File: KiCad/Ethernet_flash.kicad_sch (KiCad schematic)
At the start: 28 parts, among them IC10 MX25UM25645GXDI00-T, IC8 TFP410PAP, IC9 TS3DV642A0RUAR

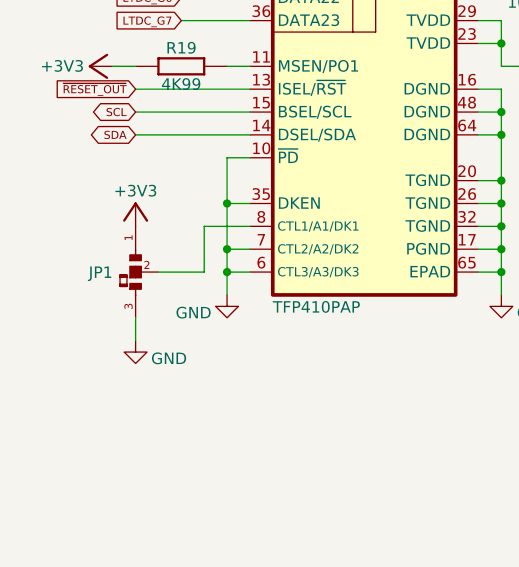
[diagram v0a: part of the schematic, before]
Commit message: JP1 type modifed
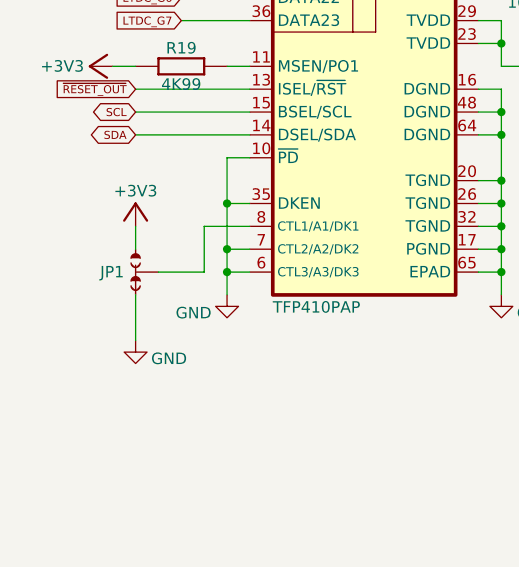
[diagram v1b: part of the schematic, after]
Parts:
- JP1: footprint PCM_EEZ_SMD:JP3 shorted with 0R (0603) 2-3 -> PCM_EEZ_SMD:JP3 shorted (0603); symbol PCM_EEZ_unsorted:JP3 shorted with 0R (2-3) -> PCM_EEZ_unsorted:JP3 shorted
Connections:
- net +3V3: now also JP1.NO; no longer JP1.1
- net GND: now also JP1.NC; no longer JP1.3
- net at IC8.8 (CTL1/A1/DK1): now also JP1.COM; no longer JP1.2
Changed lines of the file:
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@@
 	(wire
 		(pts
+			(xy 22.86 142.24) (xy 22.86 144.78)
+		)
+		(stroke
+			(width 0)
+			(type default)
+		)
+	)
+	(wire
+		(pts
 			(xy 30.48 43.18) (xy 35.56 43.18)
 		)
@@
 	(wire
 		(pts
-			(xy 22.86 152.4) (xy 22.86 154.94)
-		)
-		(stroke
-			(width 0)
-			(type default)
-		)
-	)
-	(wire
-		(pts
 			(xy 60.96 63.5) (xy 68.58 63.5)
 		)
@@
 	(wire
 		(pts
+			(xy 22.86 149.86) (xy 22.86 154.94)
+		)
+		(stroke
+			(width 0)
+			(type default)
+		)
+	)
+	(wire
+		(pts
 			(xy 60.96 43.18) (xy 68.58 43.18)
 		)
@@
 	)
 	(symbol
-		(lib_id "PCM_EEZ_unsorted:JP3 shorted with 0R (2-3)")
-		(at 22.86 147.32 90)
-		(mirror x)
+		(lib_id "PCM_EEZ_unsorted:JP3 shorted")
+		(at 22.86 147.32 0)
 		(unit 1)
 		(exclude_from_sim no)
@@
 		(on_board yes)
 		(dnp no)
-		(fields_autoplaced yes)
 		(property "Reference" "JP1"
-			(at 20.32 147.3834 90)
+			(at 21.59 147.3199 0)
 			(effects
 				(font
 					(size 1.27 1.27)
 				)
-				(justify left)
+				(justify right)
 			)
 		)
@@
 			)
 		)
-		(property "Footprint" "PCM_EEZ_SMD:JP3 shorted with 0R (0603) 2-3"
-			(at 26.67 147.32 0)
+		(property "Footprint" "PCM_EEZ_SMD:JP3 shorted (0603)"
+			(at 22.86 152.4 0)
 			(effects
 				(font
@@
 		)
 		(property "Datasheet" ""
-			(at 22.86 147.32 90)
+			(at 22.86 147.32 0)
 			(effects
 				(font
@@
 			)
 		)
-		(pin "1"
+		(property "DigiKey" ""
+			(at 22.86 147.32 0)
+			(effects
+				(font
+					(size 1.27 1.27)
+				)
+				(hide yes)
+			)
 		)
-		(pin "3"
+		(property "Mouser" ""
+			(at 22.86 147.32 0)
+			(effects
+				(font
+					(size 1.27 1.27)
+				)
+				(hide yes)
+			)
 		)
-		(pin "2"
+		(property "TME" ""
+			(at 22.86 147.32 0)
+			(effects
+				(font
+					(size 1.27 1.27)
+				)
+				(hide yes)
+			)
+		)
+		(property "LCSC" ""
+			(at 22.86 147.32 0)
+			(effects
+				(font
+					(size 1.27 1.27)
+				)
+				(hide yes)
+			)
+		)
+		(pin "COM"
+		)
+		(pin "NC"
+		)
+		(pin "NO"
 		)
 		(instances

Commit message: Folders paths adjusted, Cin added to 3V3 LDO
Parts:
- renumbered C60 to C61, C61 to C62, C62 to C63, C63 to C64, C64 to C65, C65 to C66, C66 to C67, C67 to C68, C68 to C69, C69 to C70, C70 to C71, C71 to C72, C72 to C73, C73 to C74, C74 to C75
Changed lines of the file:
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@@
 	(title_block
 		(title "${project_name}")
-		(date "2025-11-02")
+		(date "2025-11-03")
 		(rev "${project_version}")
 		(company "${project_creator}")
@@
 		(on_board yes)
 		(dnp no)
-		(property "Reference" "C61"
+		(property "Reference" "C62"
 			(at 68.58 114.3 0)
 			(effects
@@
 			(project "BB3plus CM5 STM32H7 module"
 				(path "/1a4f0aea-3a69-423f-8790-3103cd0321c4/6c545e17-ca5e-4b04-9dff-4169dbe59c9e"
-					(reference "C61")
+					(reference "C62")
 					(unit 1)
 				)
@@
 		(on_board yes)
 		(dnp no)
-		(property "Reference" "C71"
+		(property "Reference" "C72"
 			(at 256.54 38.1 0)
 			(effects
@@
 			(project "BB3plus CM5 STM32H7 module"
 				(path "/1a4f0aea-3a69-423f-8790-3103cd0321c4/6c545e17-ca5e-4b04-9dff-4169dbe59c9e"
-					(reference "C71")
+					(reference "C72")
 					(unit 1)
 				)
@@
 		(on_board yes)
 		(dnp no)
-		(property "Reference" "C64"
+		(property "Reference" "C65"
 			(at 73.66 127 0)
 			(effects
@@
 			(project "BB3plus CM5 STM32H7 module"
 				(path "/1a4f0aea-3a69-423f-8790-3103cd0321c4/6c545e17-ca5e-4b04-9dff-4169dbe59c9e"
-					(reference "C64")
+					(reference "C65")
 					(unit 1)
 				)
@@
 		(on_board yes)
 		(dnp no)
-		(property "Reference" "C72"
+		(property "Reference" "C73"
 			(at 261.62 38.1 0)
 			(effects
@@
 			(project "BB3plus CM5 STM32H7 module"
 				(path "/1a4f0aea-3a69-423f-8790-3103cd0321c4/6c545e17-ca5e-4b04-9dff-4169dbe59c9e"
-					(reference "C72")
+					(reference "C73")
 					(unit 1)
 				)
@@
 		(on_board yes)
 		(dnp no)
-		(property "Reference" "#PWR015"
+		(property "Reference" "#PWR016"
 			(at 198.12 29.21 0)
 			(effects
@@
 			(project "BB3plus CM5 STM32H7 module"
 				(path "/1a4f0aea-3a69-423f-8790-3103cd0321c4/6c545e17-ca5e-4b04-9dff-4169dbe59c9e"
-					(reference "#PWR015")
+					(reference "#PWR016")
 					(unit 1)
 				)
@@
 		(on_board yes)
 		(dnp no)
-		(property "Reference" "C60"
+		(property "Reference" "C61"
 			(at 68.58 101.6 0)
 			(effects
@@
 			(project "BB3plus CM5 STM32H7 module"
 				(path "/1a4f0aea-3a69-423f-8790-3103cd0321c4/6c545e17-ca5e-4b04-9dff-4169dbe59c9e"
-					(reference "C60")
+					(reference "C61")
 					(unit 1)
 				)
@@
 		(on_board yes)
 		(dnp no)
-		(property "Reference" "C65"
+		(property "Reference" "C66"
 			(at 78.74 101.6 0)
 			(effects
@@
 			(project "BB3plus CM5 STM32H7 module"
 				(path "/1a4f0aea-3a69-423f-8790-3103cd0321c4/6c545e17-ca5e-4b04-9dff-4169dbe59c9e"
-					(reference "C65")
+					(reference "C66")
 					(unit 1)
 				)
@@
 		(on_board yes)
 		(dnp no)
-		(property "Reference" "C63"
+		(property "Reference" "C64"
 			(at 73.66 101.6 0)
 			(effects
@@
 			(project "BB3plus CM5 STM32H7 module"
 				(path "/1a4f0aea-3a69-423f-8790-3103cd0321c4/6c545e17-ca5e-4b04-9dff-4169dbe59c9e"
-					(reference "C63")
+					(reference "C64")
 					(unit 1)
 				)
@@
 		(on_board yes)
 		(dnp no)
-		(property "Reference" "C73"
+		(property "Reference" "C74"
 			(at 269.24 38.1 0)
 			(effects
@@
 			(project "BB3plus CM5 STM32H7 module"
 				(path "/1a4f0aea-3a69-423f-8790-3103cd0321c4/6c545e17-ca5e-4b04-9dff-4169dbe59c9e"
-					(reference "C73")
+					(reference "C74")
 					(unit 1)
 				)
@@
 		(on_board yes)
 		(dnp no)
-		(property "Reference" "C66"
+		(property "Reference" "C67"
 			(at 93.98 101.6 0)
 			(effects
@@
 			(project "BB3plus CM5 STM32H7 module"
 				(path "/1a4f0aea-3a69-423f-8790-3103cd0321c4/6c545e17-ca5e-4b04-9dff-4169dbe59c9e"
-					(reference "C66")
+					(reference "C67")
 					(unit 1)
 				)
@@
 		(on_board yes)
 		(dnp no)
-		(property "Reference" "C70"
+		(property "Reference" "C71"
 			(at 248.92 38.1 0)
 			(effects
@@
 			(project "BB3plus CM5 STM32H7 module"
 				(path "/1a4f0aea-3a69-423f-8790-3103cd0321c4/6c545e17-ca5e-4b04-9dff-4169dbe59c9e"
-					(reference "C70")
+					(reference "C71")
 					(unit 1)
 				)
@@
 		(on_board yes)
 		(dnp no)
-		(property "Reference" "C62"
+		(property "Reference" "C63"
 			(at 68.58 127 0)
 			(effects
@@
 			(project "BB3plus CM5 STM32H7 module"
 				(path "/1a4f0aea-3a69-423f-8790-3103cd0321c4/6c545e17-ca5e-4b04-9dff-4169dbe59c9e"
-					(reference "C62")
+					(reference "C63")
 					(unit 1)
 				)
@@
 		(on_board yes)
 		(dnp no)
-		(property "Reference" "#PWR016"
+		(property "Reference" "#PWR017"
 			(at 251.46 52.07 0)
 			(effects
@@
 			(project "BB3plus CM5 STM32H7 module"
 				(path "/1a4f0aea-3a69-423f-8790-3103cd0321c4/6c545e17-ca5e-4b04-9dff-4169dbe59c9e"
-					(reference "#PWR016")
+					(reference "#PWR017")
 					(unit 1)
 				)
@@
 		(on_board yes)
 		(dnp no)
-		(property "Reference" "C67"
+		(property "Reference" "C68"
 			(at 160.02 114.3 0)
 			(effects
@@
 			(project "BB3plus CM5 STM32H7 module"
 				(path "/1a4f0aea-3a69-423f-8790-3103cd0321c4/6c545e17-ca5e-4b04-9dff-4169dbe59c9e"
-					(reference "C67")
+					(reference "C68")
 					(unit 1)
 				)
@@
 		(on_board yes)
 		(dnp no)
-		(property "Reference" "C74"
+		(property "Reference" "C75"
 			(at 274.32 38.1 0)
 			(effects
@@
 			(project "BB3plus CM5 STM32H7 module"
 				(path "/1a4f0aea-3a69-423f-8790-3103cd0321c4/6c545e17-ca5e-4b04-9dff-4169dbe59c9e"
-					(reference "C74")
+					(reference "C75")
 					(unit 1)
 				)
@@
 		(on_board yes)
 		(dnp no)
-		(property "Reference" "#PWR017"
+		(property "Reference" "#PWR018"
 			(at 274.32 34.29 0)
 			(effects
@@
 			(project "BB3plus CM5 STM32H7 module"
 				(path "/1a4f0aea-3a69-423f-8790-3103cd0321c4/6c545e17-ca5e-4b04-9dff-4169dbe59c9e"
-					(reference "#PWR017")
+					(reference "#PWR018")
 					(unit 1)
 				)
@@
 		(on_board yes)
 		(dnp no)
-		(property "Reference" "C68"
+		(property "Reference" "C69"
 			(at 165.1 114.3 0)
 			(effects
@@
 			(project "BB3plus CM5 STM32H7 module"
 				(path "/1a4f0aea-3a69-423f-8790-3103cd0321c4/6c545e17-ca5e-4b04-9dff-4169dbe59c9e"
-					(reference "C68")
+					(reference "C69")
 					(unit 1)
 				)
@@
 		(on_board yes)
 		(dnp no)
-		(property "Reference" "C69"
+		(property "Reference" "C70"
 			(at 243.84 38.1 0)
 			(effects
@@
 			(project "BB3plus CM5 STM32H7 module"
 				(path "/1a4f0aea-3a69-423f-8790-3103cd0321c4/6c545e17-ca5e-4b04-9dff-4169dbe59c9e"
-					(reference "C69")
+					(reference "C70")
 					(unit 1)
 				)

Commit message: BOM update
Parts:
- C67, C71, C73, C75: Mouser 187-CL10A475KP8NNNC -> 187-CL10A475KP8NNND
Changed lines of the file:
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@@
 	(wire
 		(pts
-			(xy 165.1 111.76) (xy 170.18 111.76)
+			(xy 165.1 111.76) (xy 167.64 111.76)
 		)
 		(stroke
@@
 		(on_board yes)
 		(dnp no)
-		(fields_autoplaced yes)
 		(property "Reference" "IC9"
-			(at 135.89 33.02 0)
+			(at 124.46 37.465 0)
+			(do_not_autoplace yes)
 			(effects
 				(font
 					(size 1.27 1.27)
 				)
+				(justify left bottom)
 			)
 		)
 		(property "Value" "TS3DV642A0RUAR"
-			(at 135.89 35.56 0)
+			(at 124.46 120.015 0)
+			(do_not_autoplace yes)
 			(effects
 				(font
 					(size 1.27 1.27)
 				)
+				(justify left top)
 			)
 		)
@@
 			)
 		)
-		(property "Mouser" "187-CL10A475KP8NNNC"
+		(property "Mouser" "187-CL10A475KP8NNND"
 			(at 261.62 38.1 0)
 			(effects
@@
 	(symbol
 		(lib_id "PCM_EEZ_symbols:+3V3")
-		(at 172.72 111.76 270)
+		(at 170.18 111.76 270)
 		(unit 1)
 		(exclude_from_sim no)
@@
 		(dnp no)
 		(property "Reference" "#+3V019"
-			(at 172.72 111.76 0)
+			(at 170.18 111.76 0)
 			(effects
 				(font
@@
 		)
 		(property "Value" "+3V3"
-			(at 173.355 112.395 90)
+			(at 170.815 112.395 90)
 			(effects
 				(font
@@
 		)
 		(property "Footprint" ""
-			(at 172.72 111.76 0)
+			(at 170.18 111.76 0)
 			(effects
 				(font
@@
 		)
 		(property "Datasheet" ""
-			(at 172.72 111.76 0)
+			(at 170.18 111.76 0)
 			(effects
 				(font
@@
 		)
 		(property "Description" "Power symbol creates a global label with name \"+3V3\""
-			(at 172.72 111.76 0)
+			(at 170.18 111.76 0)
 			(effects
 				(font
@@
 			)
 		)
-		(property "Mouser" "187-CL10A475KP8NNNC"
+		(property "Mouser" "187-CL10A475KP8NNND"
 			(at 93.98 101.6 0)
 			(effects
@@
 			)
 		)
-		(property "Mouser" "187-CL10A475KP8NNNC"
+		(property "Mouser" "187-CL10A475KP8NNND"
 			(at 248.92 38.1 0)
 			(effects
@@
 			)
 		)
-		(property "Mouser" "187-CL10A475KP8NNNC"
+		(property "Mouser" "187-CL10A475KP8NNND"
 			(at 274.32 38.1 0)
 			(effects
